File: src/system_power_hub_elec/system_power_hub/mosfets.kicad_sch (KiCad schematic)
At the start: 19 parts, among them J2 XT60F, J4 XT60F, Q2 Q_Dual_NPN_NPN_E1B1C2E2B2C1, Q3 IRFH7440TRPBF, Q4 IRFH7440TRPBF

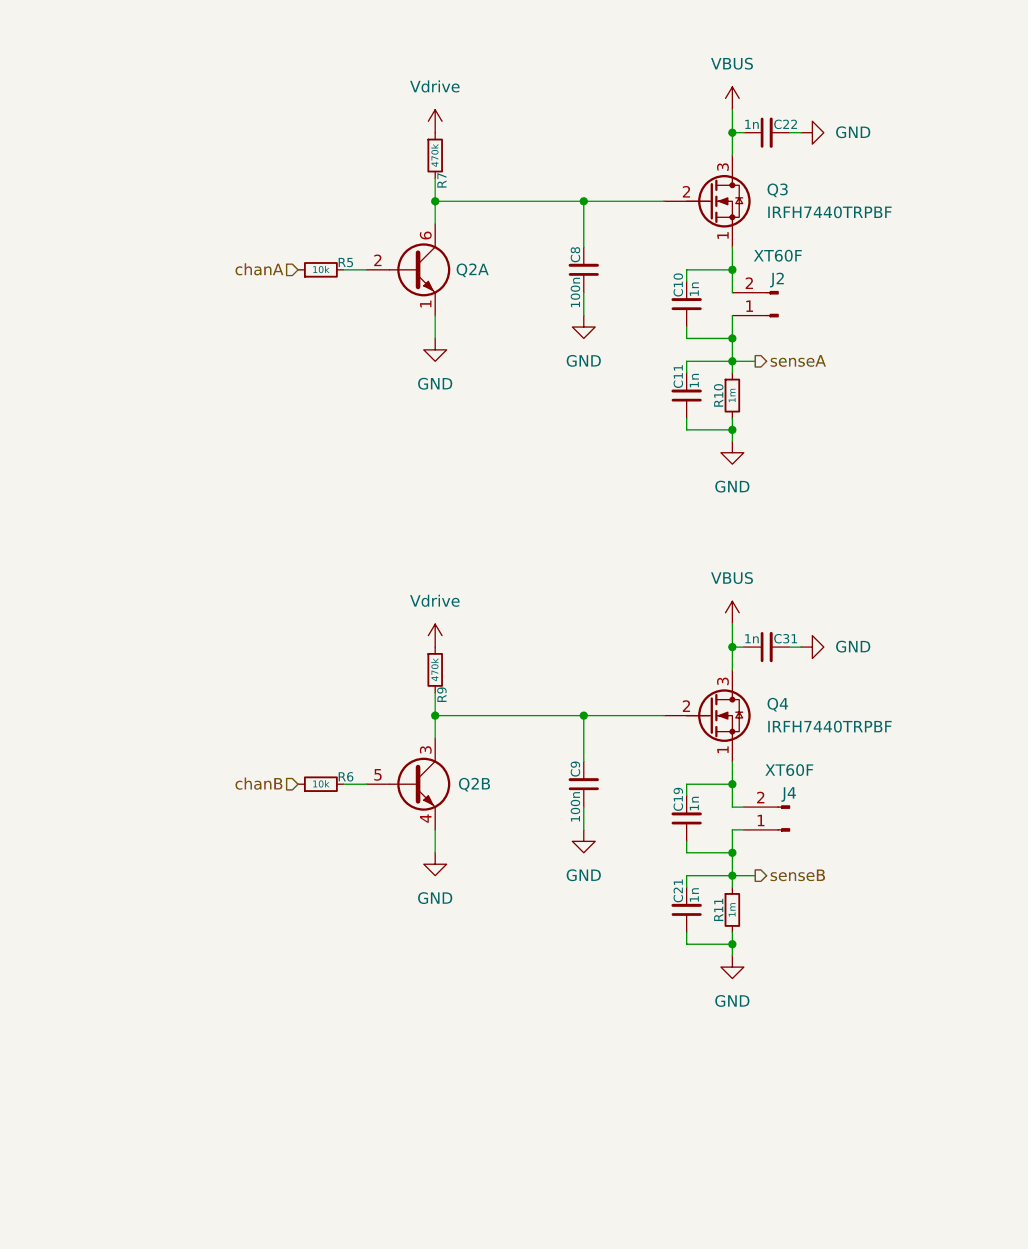
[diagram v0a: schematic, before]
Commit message: [WIP] Copied KiCAD proj from MPM, modified schematic for SPM
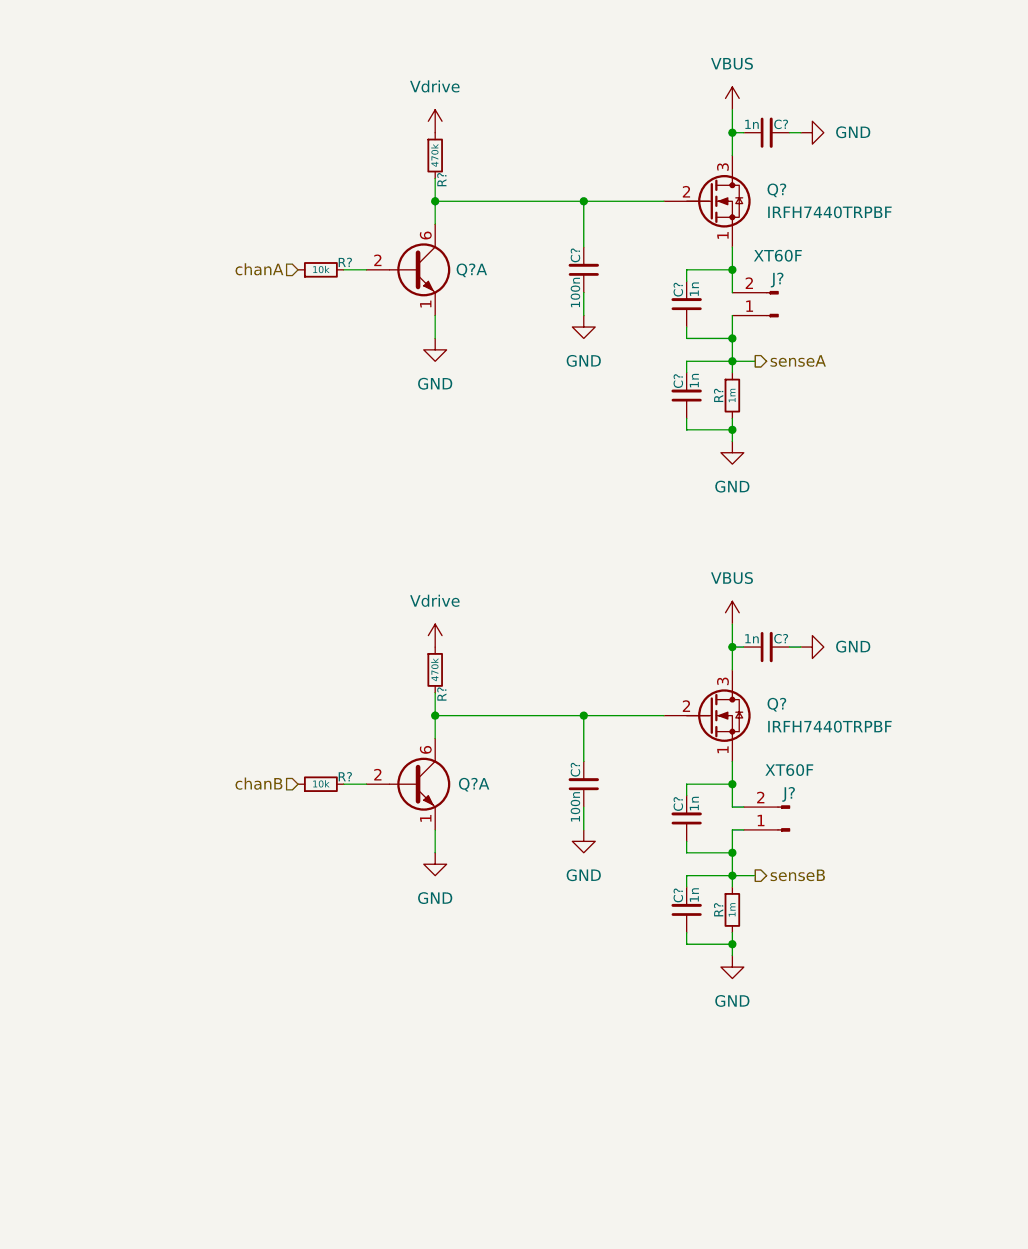
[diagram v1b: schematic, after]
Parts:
- renumbered C22 to C?, C21 to C?, C9 to C?, C19 to C?, C11 to C?, C31 to C?, C8 to C?, C10 to C?, J4 to J?, J2 to J?, Q3 to Q?, Q2 to Q?, Q4 to Q?, R6 to R?, R9 to R?, R10 to R?, R11 to R?, R5 to R?, R7 to R?
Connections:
- net GND: now also Q?.1 (E1); no longer Q?.4 (E2)
- net at R?.2: now also Q?.2 (B1); no longer Q?.5 (B2)
- net at C?.2, Q?.2 (G), R?.2: now also Q?.6 (C1); no longer Q?.3 (C2)

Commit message: Draft SPM PCB layout
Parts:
- J2, J4: renamed from J?; value XT60F -> XT30F; footprint Connector_AMASS:AMASS_XT60PW-F_1x02_P7.20mm_Horizontal -> Connector_AMASS:AMASS_XT30PW-F_1x02_P2.50mm_Horizontal
- gave numbers to parts that had none: 17
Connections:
- net GND: now also Q2.4 (E2); no longer Q2.1 (E1)
- net at R6.2: now also Q2.5 (B2); no longer Q2.2 (B1)
- net at C9.2, Q12.2 (G), R9.2: now also Q2.3 (C2); no longer Q2.6 (C1)

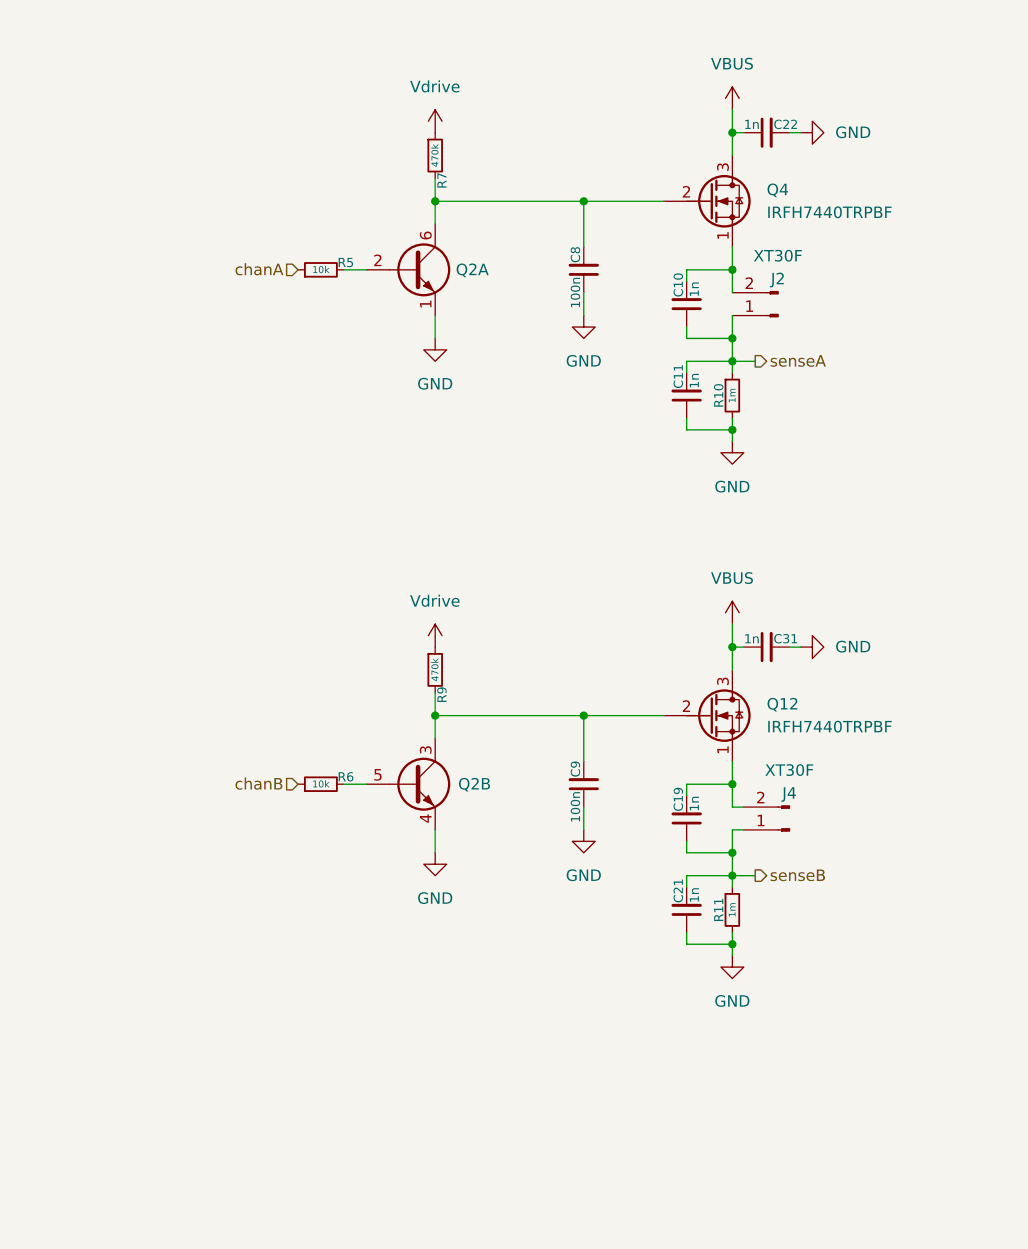
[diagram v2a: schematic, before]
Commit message: Fix SPM schematic as per errata 04-02-2026
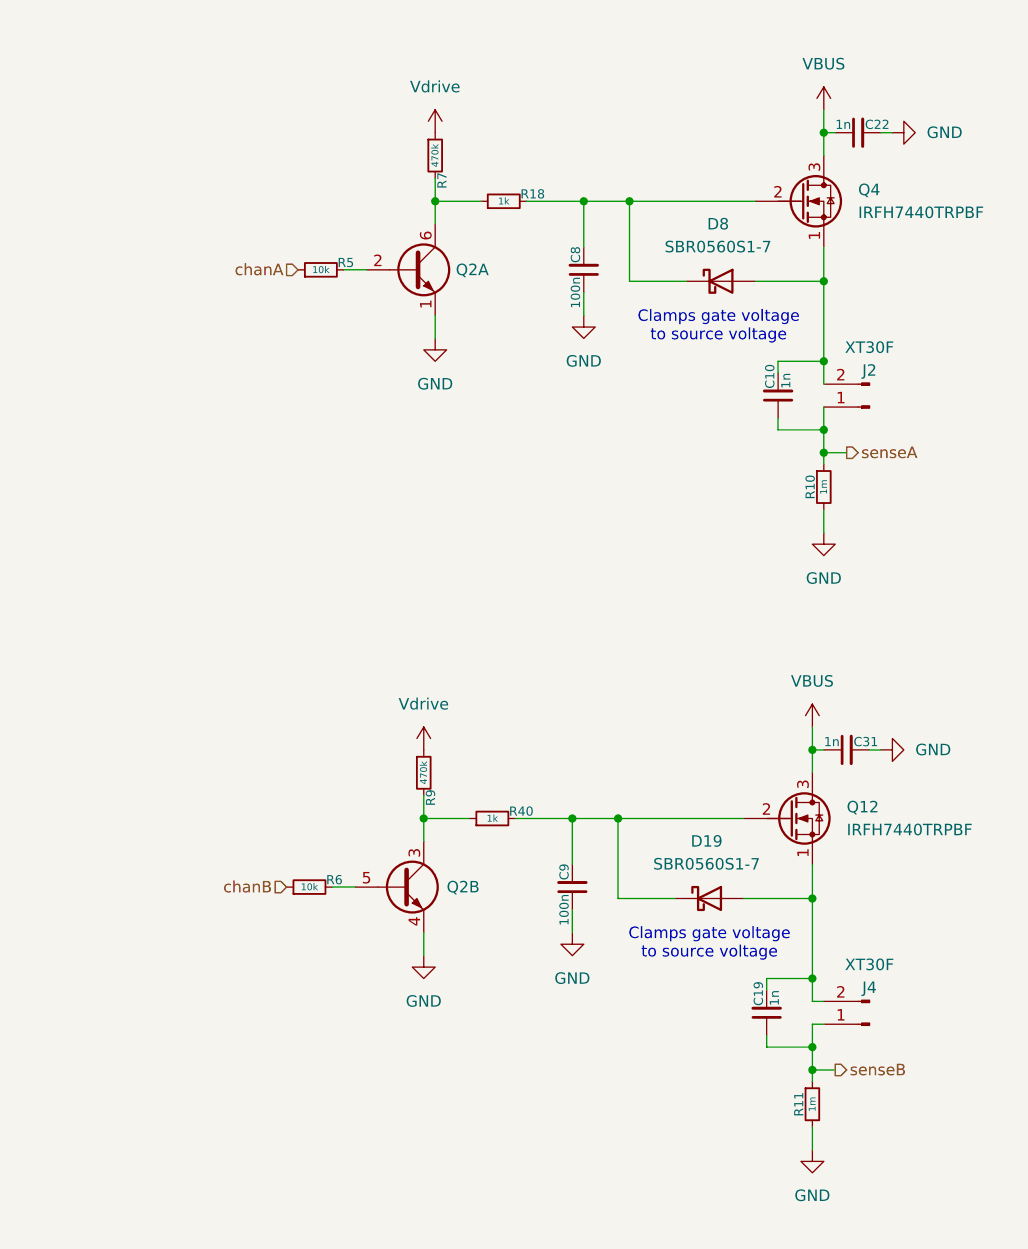
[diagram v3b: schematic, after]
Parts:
- removed C11, C21: 1n, Capacitor_SMD:C_0402_1005Metric, symbol Bluesat:C_CompactV
- added D19, D8: SBR0560S1-7, Diode_SMD:D_SOD-123, symbol Device:D_Schottky
- added R18, R40: 1k, Resistor_SMD:R_0402_1005Metric, symbol Bluesat:R_CompactH
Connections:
- net at C19.2, J4.2 (Pin_2), Q12.1 (S): now also D19.2 (A)
- net at C10.2, J2.2 (Pin_2), Q4.1 (S): now also D8.2 (A)
- net at C8.2, Q4.2 (G): now also D8.1 (K), R18.2; no longer Q2.6 (C1), R7.2
- net at Q2.3 (C2), R9.2: now also R40.1; no longer C9.2, Q12.2 (G)
- new net: Q2.6 (C1), R18.1, R7.2
- new net: C9.2, D19.1 (K), Q12.2 (G), R40.2
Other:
- note added: "Clamps gate voltage to source voltage"
- moved on the sheet: C10, C19, C22, C31, C9, J2, J4, Q12, Q2B, Q4, R10, R11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

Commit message: Cleaned up routing and adjusted PCB layout
- Moved components at least 1.5mm away from board edge
- Adjusted board size slightly for more clearance
- Removed pullups for eeprom
- Adjusted via sizing, made some smaller
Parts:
- removed C22, C31: 1n, Capacitor_SMD:C_0402_1005Metric, symbol Bluesat:C_CompactH

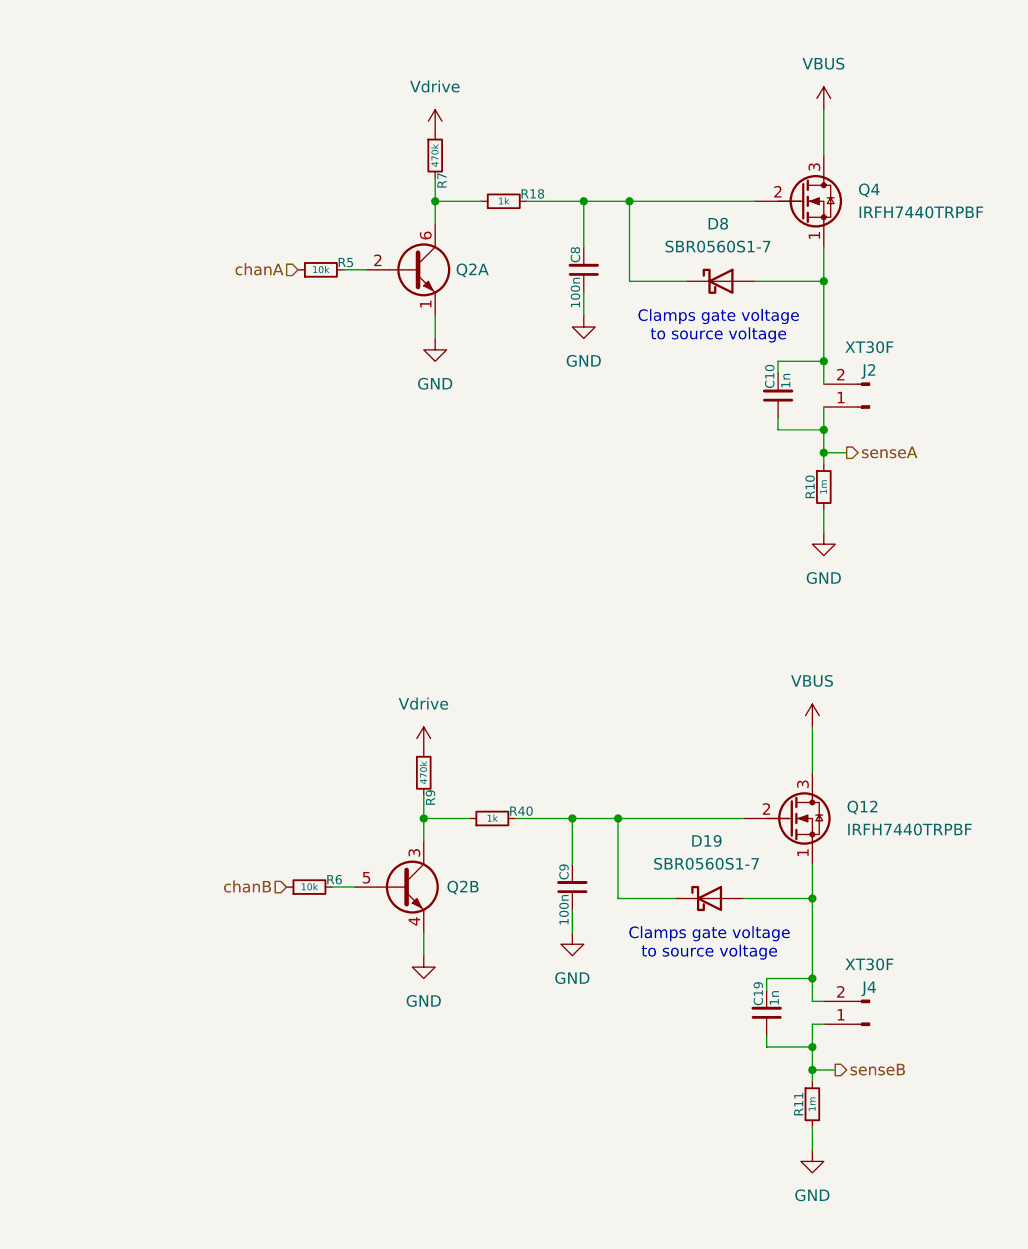
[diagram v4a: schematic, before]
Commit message: Updated SPM channels to reflect MPM changes
- Added schottky to vdrive path
- Modified schottky diodes to be sod 882 (SBR0240LP-7)
- Changed 100n capacitor connection to NMOS source
- Updated routing accordingly
- Minor DRC fixes
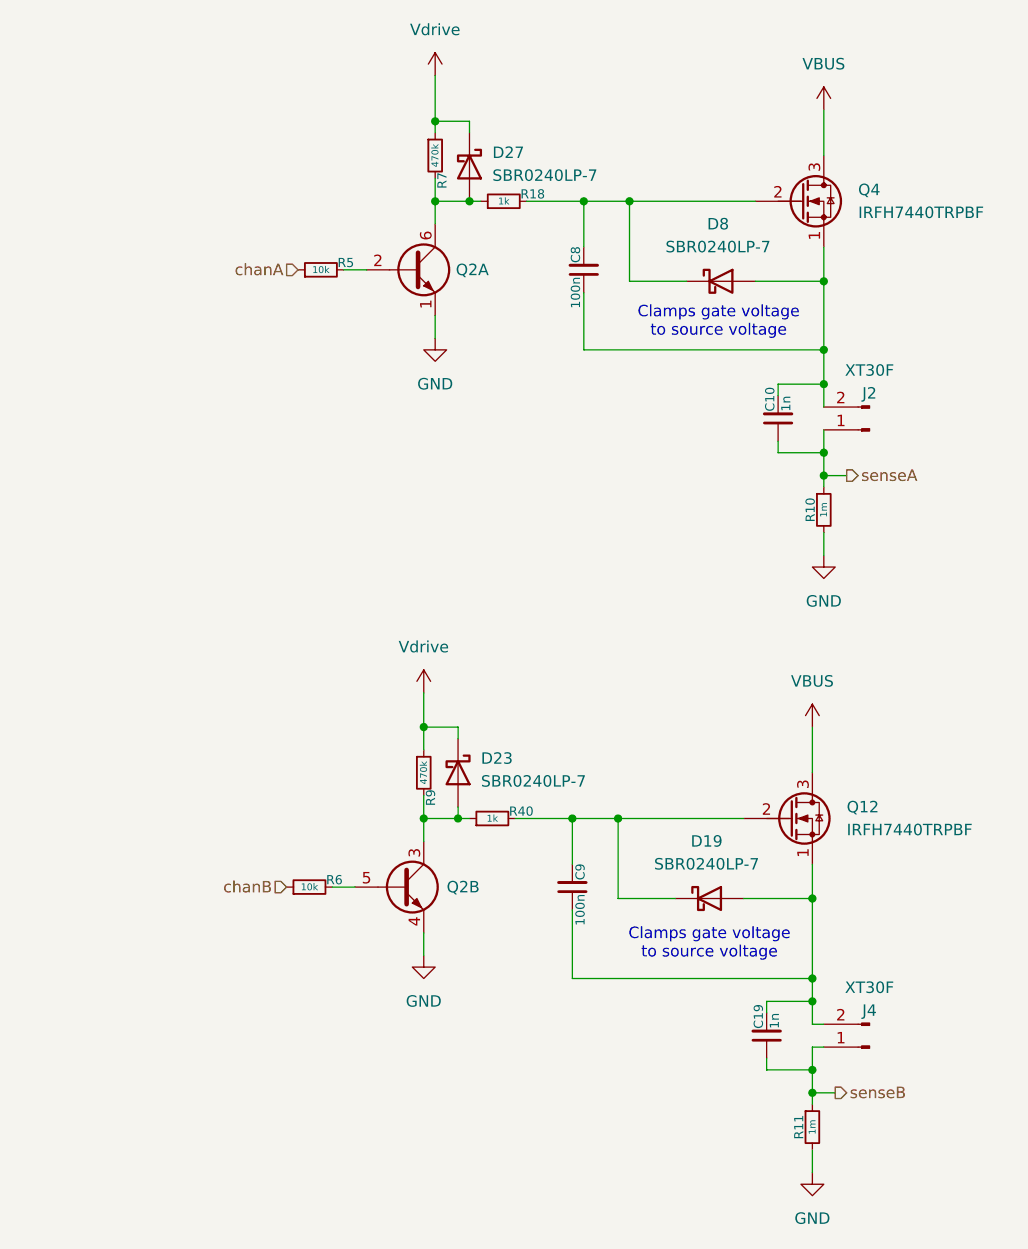
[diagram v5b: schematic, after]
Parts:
- added D23, D27: SBR0240LP-7, Diode_SMD:D_SOD-882D, symbol Device:D_Schottky
- D19, D8: value SBR0560S1-7 -> SBR0240LP-7; footprint Diode_SMD:D_SOD-123 -> Diode_SMD:D_SOD-882D
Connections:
- net GND: no longer C8.1, C9.1
- net Vdrive: now also D23.1 (K), D27.1 (K)
- net at C19.2, D19.2 (A), J4.2 (Pin_2)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: now also C9.1
- net at C10.2, D8.2 (A), J2.2 (Pin_2)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: now also C8.1
- net at Q2.6 (C1), R18.1, R7.2: now also D27.2 (A)
- net at Q2.3 (C2), R40.1, R9.2: now also D23.2 (A)
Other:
- moved on the sheet: C10, C19, C9, J2, J4, R10, R11

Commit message: Prepattern
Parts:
- removed Q12, Q4: IRFH7440TRPBF, Bluesat:PQFN_5x6mm_E_SGD, symbol Transistor_FET:Q_NMOS_SGD
- added Q201, Q202: IRFH7440TRPBF, Bluesat:PQFN_5x6mm_E_DGS, symbol Transistor_FET:Q_NMOS_DGS
- C8, C9: footprint Capacitor_SMD:C_0603_1608Metric -> Capacitor_SMD:C_0402_1005Metric
- D19, D23, D27, D8: footprint Diode_SMD:D_SOD-882D -> Diode_SMD:D_SOD-882
- Q2: footprint Package_TO_SOT_SMD:SOT-363_SC-70-6 -> Bluesat:SOT-363
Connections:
- net VBUS: now also Q201.1 (D), Q202.1 (D)
- net OUT_{B}: now reaches C19.2, C9.1, D19.2 (A), J4.2 (Pin_2)
- net OUT_{B}: now also Q202.3 (S)
- net OUT_{A}: now reaches C10.2, C8.1, D8.2 (A), J2.2 (Pin_2)
- net OUT_{A}: now also Q201.3 (S)
- net GATE_{A}: now reaches C8.2, D8.1 (K), R18.2
- net GATE_{A}: now also Q201.2 (G)
- net CTRL_{A}: now reaches D27.2 (A), Q2.6 (C1), R18.1, R7.2
- net CTRL_{B}: now reaches D23.2 (A), Q2.3 (C2), R40.1, R9.2
- net GATE_{B}: now reaches C9.2, D19.1 (K), R40.2
- net GATE_{B}: now also Q202.2 (G)

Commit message: Finish layout
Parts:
- added H301: MountingHole, Bluesat:M2.5_Internal, symbol Mechanical:MountingHole
- renumbered C8 to C301, C10 to C302, C9 to C303, C19 to C304, D27 to D301, D8 to D302, D23 to D303, D19 to D304, J2 to J301, J4 to J302, Q201 to Q301, Q2 to Q302, Q202 to Q303, R7 to R301, R18 to R302, R5 to R303, R10 to R304, R9 to R305, R40 to R306, R6 to R307, R11 to R308
